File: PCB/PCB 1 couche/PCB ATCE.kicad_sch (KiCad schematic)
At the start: 29 parts, among them J1 USB_OTG, J2 Conn_Coaxial, SW1 SW_Push, SW2 SW_Push, U2 ${SIM.PARAMS}, Y1 16MHz

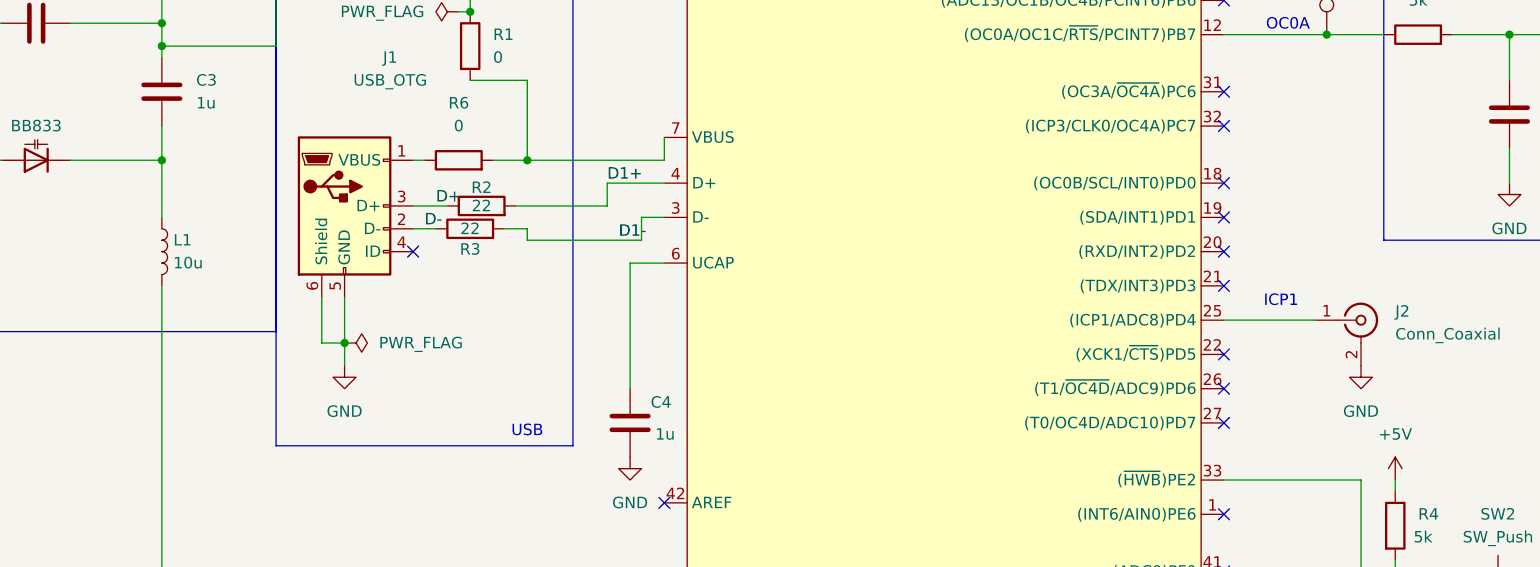
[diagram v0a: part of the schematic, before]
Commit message: Passage des fichiers KiCAD à la version 9
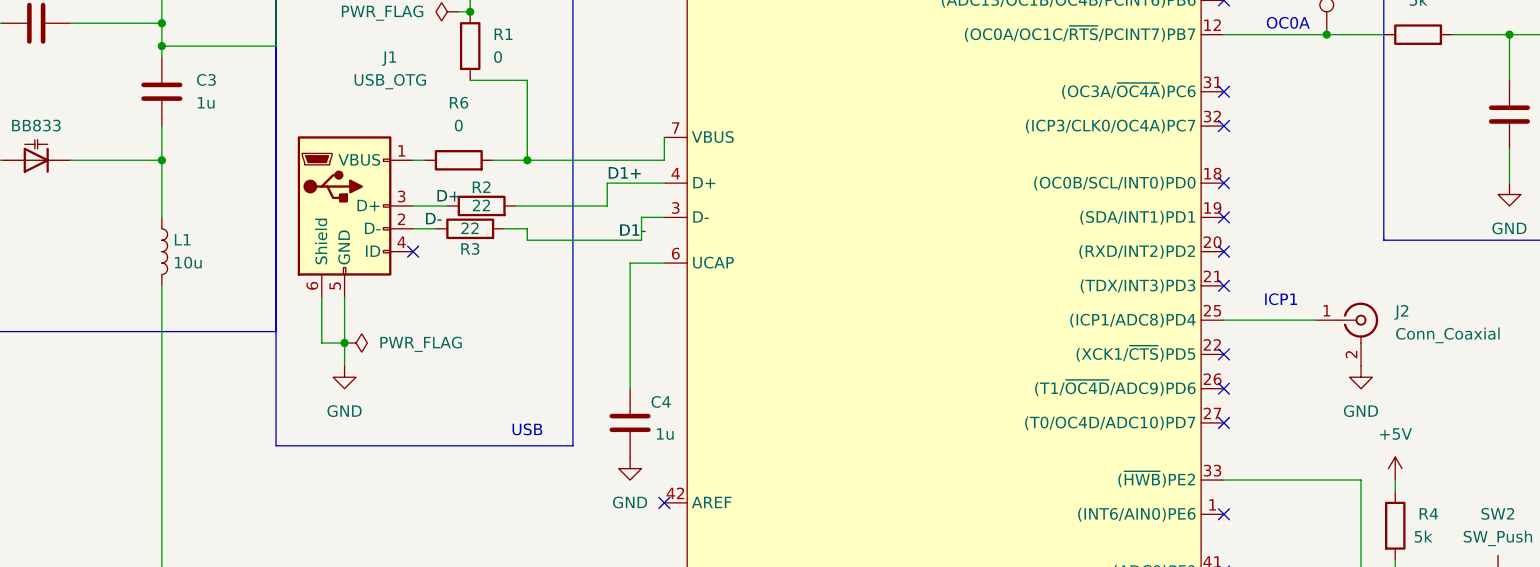
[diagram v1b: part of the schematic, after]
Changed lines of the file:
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@@
 (kicad_sch
-	(version 20231120)
+	(version 20250114)
 	(generator "eeschema")
-	(generator_version "8.0")
+	(generator_version "9.0")
 	(paper "A4")
 	(title_block
@@
 		(company "Paul ROUSSEAU")
 	)
+	(rectangle
+		(start 181.61 60.96)
+		(end 203.835 93.98)
+		(stroke
+			(width 0)
+			(type default)
+		)
+		(fill
+			(type none)
+		)
+	)
+	(rectangle
+		(start 217.805 57.15)
+		(end 247.65 90.805)
+		(stroke
+			(width 0)
+			(type default)
+		)
+		(fill
+			(type none)
+		)
+	)
+	(rectangle
+		(start 224.79 14.605)
+		(end 271.78 43.18)
+		(stroke
+			(width 0)
+			(type default)
+		)
+		(fill
+			(type none)
+		)
+	)
+	(rectangle
+		(start 58.42 64.77)
+		(end 91.44 116.84)
+		(stroke
+			(width 0)
+			(type default)
+		)
+		(fill
+			(type none)
+		)
+	)
+	(rectangle
+		(start 16.51 43.18)
+		(end 58.42 104.14)
+		(stroke
+			(width 0)
+			(type default)
+		)
+		(fill
+			(type none)
+		)
+	)
+	(text "ICP1"
+		(exclude_from_sim no)
+		(at 170.18 100.838 0)
+		(effects
+			(font
+				(size 1.27 1.27)
+			)
+		)
+	)
+	(text "Filtre"
+		(exclude_from_sim no)
+		(at 199.39 63.246 0)
+		(effects
+			(font
+				(size 1.27 1.27)
+			)
+		)
+	)
+	(text "USB"
+		(exclude_from_sim no)
+		(at 86.36 115.316 0)
+		(effects
+			(font
+				(size 1.27 1.27)
+			)
+		)
+	)
+	(text "Résonateur"
+		(exclude_from_sim no)
+		(at 52.07 45.72 0)
+		(effects
+			(font
+				(size 1.27 1.27)
+			)
+		)
+	)
+	(text "Suiveur"
+		(exclude_from_sim no)
+		(at 242.062 60.96 0)
+		(effects
+			(font
+				(size 1.27 1.27)
+			)
+		)
+	)
+	(text "OC0A"
+		(exclude_from_sim no)
+		(at 170.942 70.104 0)
+		(effects
+			(font
+				(size 1.27 1.27)
+			)
+		)
+	)
+	(text "Découplage\nalimentation"
+		(exclude_from_sim no)
+		(at 262.128 18.034 0)
+		(effects
+			(font
+				(size 1.27 1.27)
+			)
+		)
+	)
 	(junction
 		(at 86.36 85.09)
@@
 		)
 	)
-	(rectangle
-		(start 181.61 60.96)
-		(end 203.835 93.98)
-		(stroke
-			(width 0)
-			(type default)
-		)
-		(fill
-			(type none)
-		)
-	)
-	(rectangle
-		(start 217.805 57.15)
-		(end 247.65 90.805)
-		(stroke
-			(width 0)
-			(type default)
-		)
-		(fill
-			(type none)
-		)
-	)
-	(rectangle
-		(start 224.79 14.605)
-		(end 271.78 43.18)
-		(stroke
-			(width 0)
-			(type default)
-		)
-		(fill
-			(type none)
-		)
-	)
-	(rectangle
-		(start 58.42 64.77)
-		(end 91.44 116.84)
-		(stroke
-			(width 0)
-			(type default)
-		)
-		(fill
-			(type none)
-		)
-	)
-	(rectangle
-		(start 16.51 43.18)
-		(end 58.42 104.14)
-		(stroke
-			(width 0)
-			(type default)
-		)
-		(fill
-			(type none)
-		)
-	)
-	(text "ICP1"
-		(exclude_from_sim no)
-		(at 170.18 100.838 0)
-		(effects
-			(font
-				(size 1.27 1.27)
-			)
-		)
-	)
-	(text "Filtre"
-		(exclude_from_sim no)
-		(at 199.39 63.246 0)
-		(effects
-			(font
-				(size 1.27 1.27)
-			)
-		)
-	)
-	(text "USB"
-		(exclude_from_sim no)
-		(at 86.36 115.316 0)
-		(effects
-			(font
-				(size 1.27 1.27)
-			)
-		)
-	)
-	(text "Résonateur"
-		(exclude_from_sim no)
-		(at 52.07 45.72 0)
-		(effects
-			(font
-				(size 1.27 1.27)
-			)
-		)
-	)
-	(text "Suiveur"
-		(exclude_from_sim no)
-		(at 242.062 60.96 0)
-		(effects
-			(font
-				(size 1.27 1.27)
-			)
-		)
-	)
-	(text "OC0A"
-		(exclude_from_sim no)
-		(at 170.942 70.104 0)
-		(effects
-			(font
-				(size 1.27 1.27)
-			)
-		)
-	)
-	(text "Découplage\nalimentation"
-		(exclude_from_sim no)
-		(at 262.128 18.034 0)
-		(effects
-			(font
-				(size 1.27 1.27)
-			)
-		)
-	)
 	(label "D-"
 		(at 74.93 92.71 0)
@@
 		)
 	)
+	(embedded_fonts no)
 )

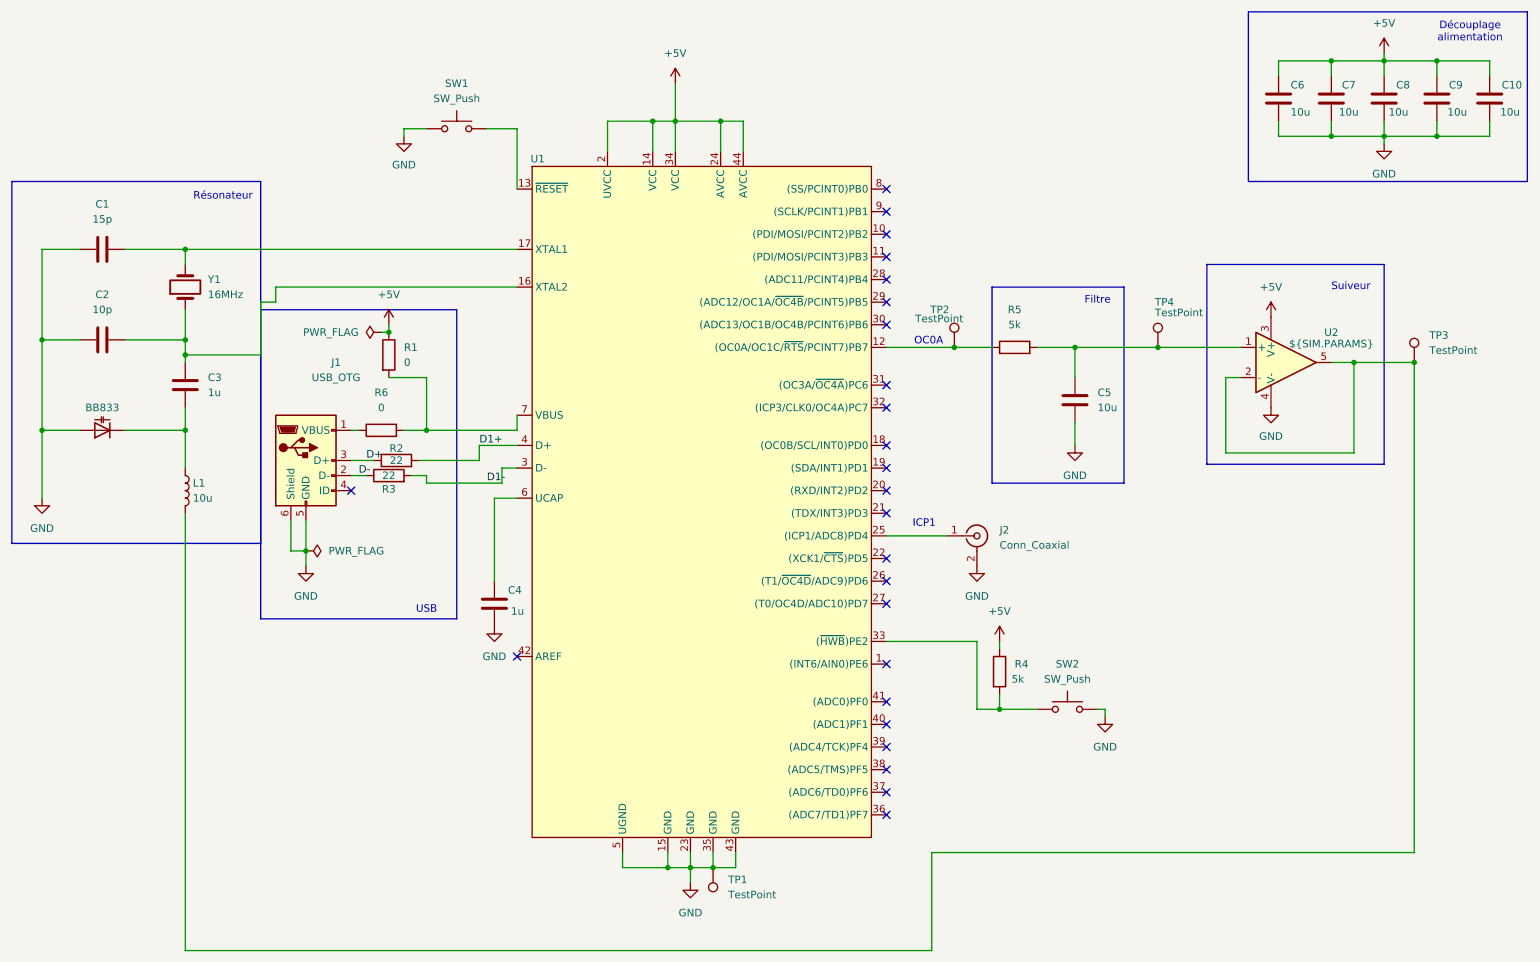
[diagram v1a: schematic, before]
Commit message: Changement des ports pour le PWM et l'ICP
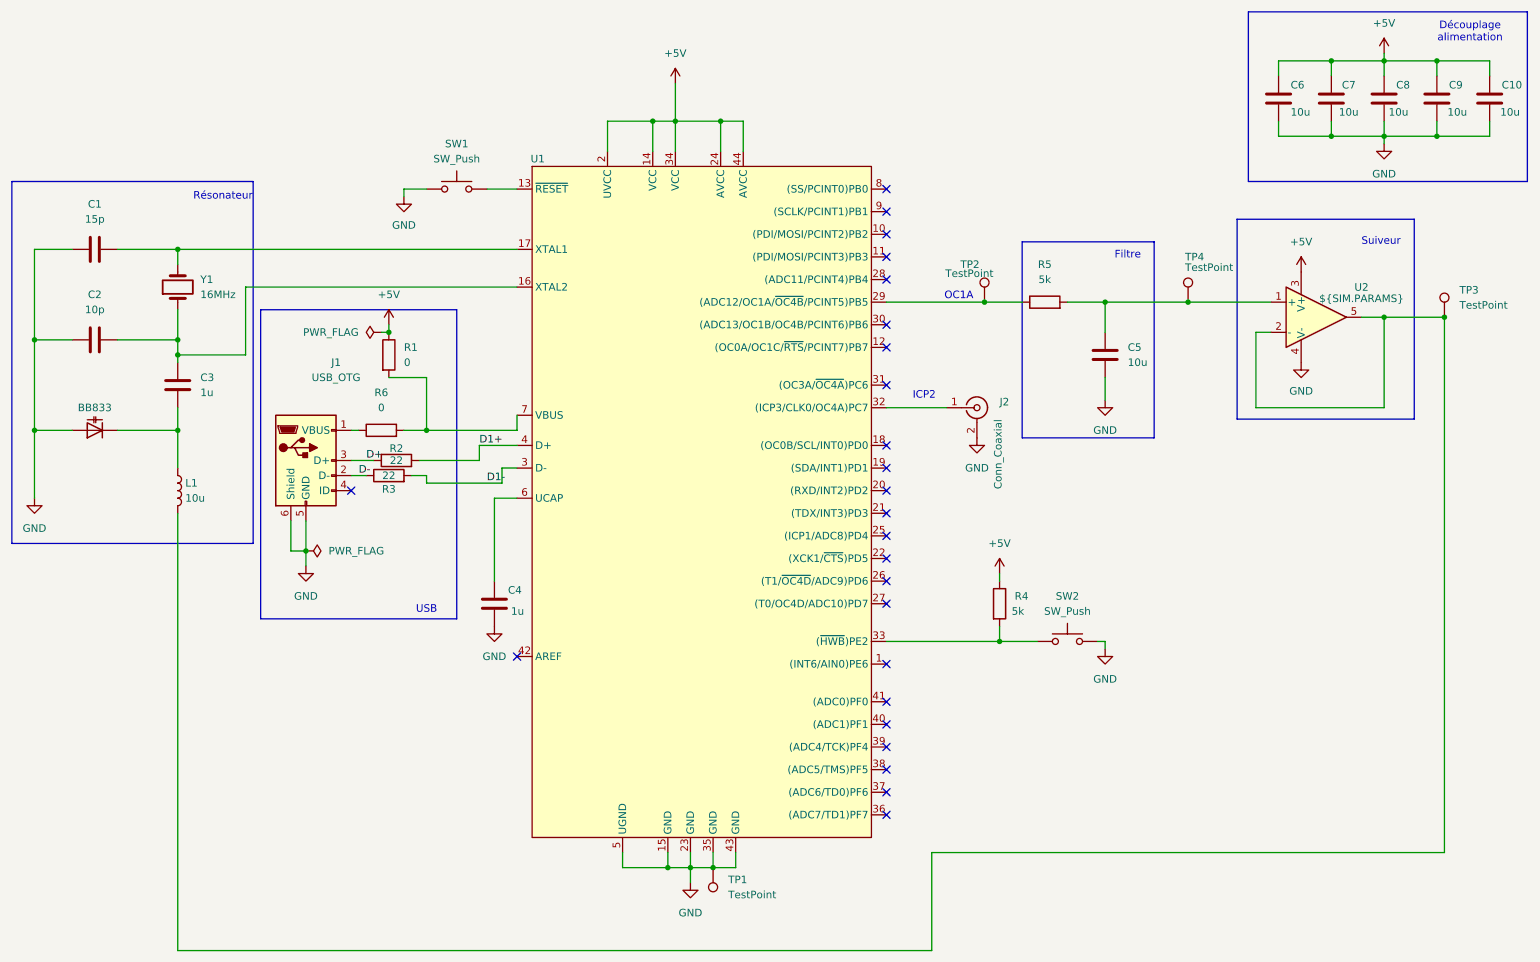
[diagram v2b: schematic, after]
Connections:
- net at R5.1, TP2.1: now also U1.29 ((ADC12/OC1A/~{OC4B}/PCINT5)PB5); no longer U1.12 ((OC0A/OC1C/~{RTS}/PCINT7)PB7)
- net at U1.25 ((ICP1/ADC8)PD4): no longer J2.1 (In)
- net at U1.32 ((ICP3/CLK0/OC4A)PC7): now also J2.1 (In)
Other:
- note added: "ICP2"
- note added: "OC1A"
- note removed: "ICP1"
- note removed: "OC0A"
- moved on the sheet: BB833, C1, C2, C3, C5, J2, L1, R4, R5, SW1, SW2, TP2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

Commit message: modification pcb (empreinte test point + routage nouveau pwm)
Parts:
- TP1, TP2, TP3, TP4: footprint TestPoint:TestPoint_Keystone_5000-5004_Miniature -> TestPoint:TestPoint_Pad_D1.5mm
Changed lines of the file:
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@@
 			)
 		)
-		(property "Footprint" "TestPoint:TestPoint_Keystone_5000-5004_Miniature"
+		(property "Footprint" "TestPoint:TestPoint_Pad_D1.5mm"
 			(at 219.71 63.5 0)
 			(effects
@@
 			)
 		)
-		(property "Footprint" "TestPoint:TestPoint_Keystone_5000-5004_Miniature"
+		(property "Footprint" "TestPoint:TestPoint_Pad_D1.5mm"
 			(at 129.54 158.75 0)
 			(effects
@@
 			)
 		)
-		(property "Footprint" "TestPoint:TestPoint_Keystone_5000-5004_Miniature"
+		(property "Footprint" "TestPoint:TestPoint_Pad_D1.5mm"
 			(at 185.42 63.5 0)
 			(effects
@@
 			)
 		)
-		(property "Footprint" "TestPoint:TestPoint_Keystone_5000-5004_Miniature"
+		(property "Footprint" "TestPoint:TestPoint_Pad_D1.5mm"
 			(at 262.89 66.04 0)
 			(effects
